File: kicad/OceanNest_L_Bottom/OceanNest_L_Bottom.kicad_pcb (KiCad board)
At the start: 2 copper layers, 103.5 x 88.7 mm, 4 parts

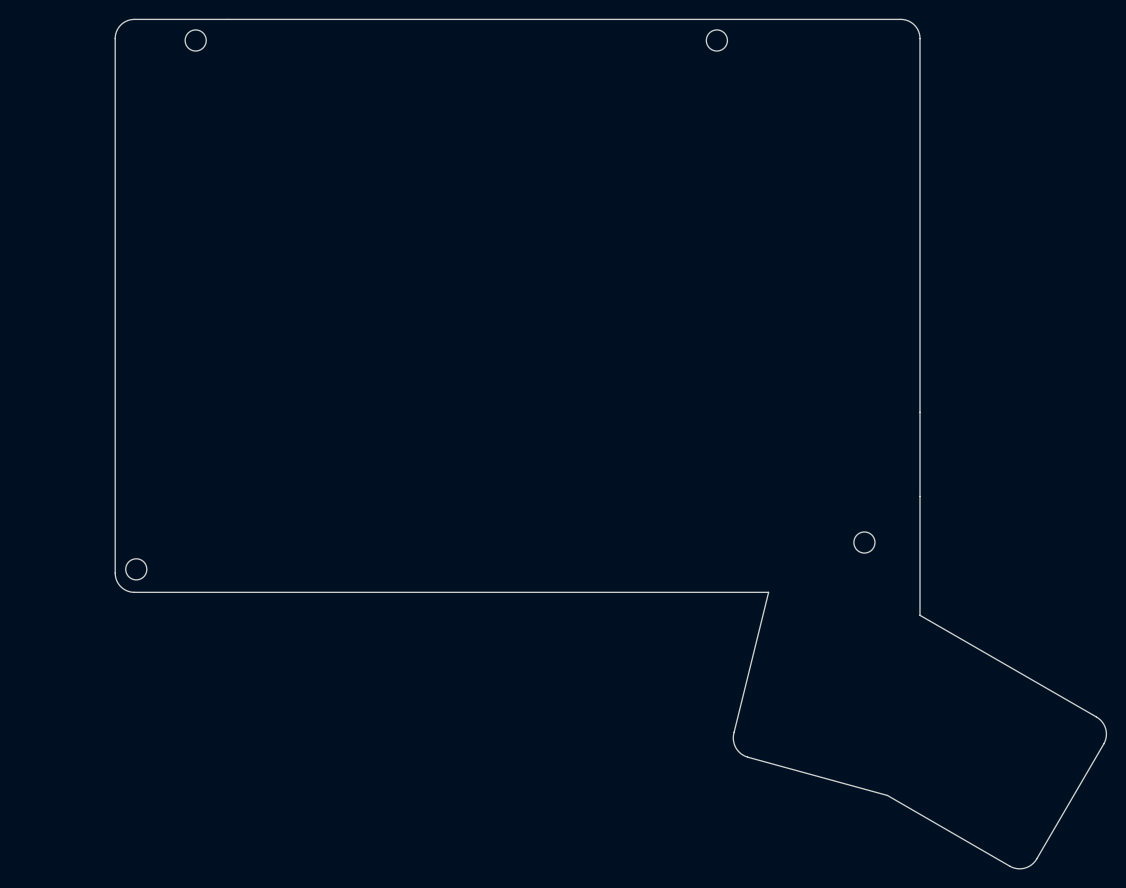
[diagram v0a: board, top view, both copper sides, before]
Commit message: feat: add new OceanNest_L and OceanNest_R PCB and project files for enhanced design capabilities
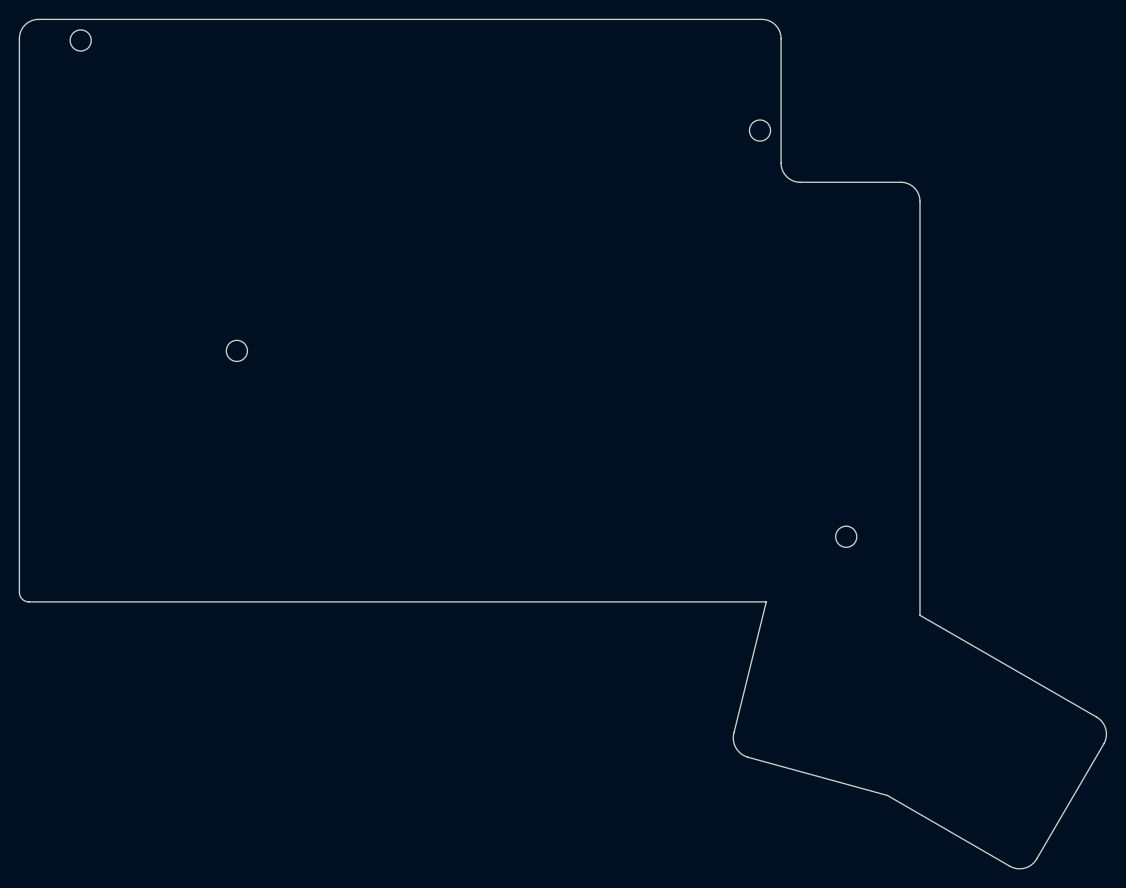
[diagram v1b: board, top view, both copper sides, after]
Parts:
- removed Ref** (x3): Val**, isw-kbd:M2_ScrewHole
- added hole2: Val**, kbd_Hole:m2_Screw_Hole, F.Cu at (72.7, 134.6)
- added hole2: Val**, kbd_Hole:m2_Screw_Hole, F.Cu at (127.3, 111.6)
- added hole2: Val**, kbd_Hole:m2_Screw_Hole, F.Cu at (56.4, 102.2)
- hole1: renamed from Ref**; footprint isw-kbd:M2_ScrewHole -> kbd_Hole:m2_Screw_Hole
- moved hole1 1.99 mm to (136.3, 154.0)
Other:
- board size 103.5 x 88.7 mm -> 113.5 x 88.7 mm
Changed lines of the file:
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@@
 	)
 	(net 0 "")
-	(footprint "isw-kbd:M2_ScrewHole"
+	(footprint "kbd_Hole:m2_Screw_Hole"
 		(layer "F.Cu")
-		(at 62.2 157.4)
+		(at 72.7 134.6)
 		(descr "Mounting Hole 2.2mm, no annular, M2")
 		(tags "mounting hole 2.2mm no annular m2")
-		(property "Reference" "Ref**"
-			(at 0 3 0)
-			(layer "F.Fab")
-			(hide yes)
+		(property "Reference" "hole2"
+			(at 0 -3.2 0)
+			(layer "F.Fab")
 			(effects
 				(font
@@
 		)
 		(property "Value" "Val**"
-			(at 0 -3 0)
-			(layer "F.Fab")
-			(hide yes)
+			(at 0 3.2 0)
+			(layer "F.Fab")
 			(effects
 				(font
@@
 		(fp_circle
 			(center 0 0)
-			(end 2 0)
+			(end 2.2 0)
 			(stroke
 				(width 0.15)
@@
 			)
 			(fill no)
-			(layer "B.Fab")
+			(layer "Cmts.User")
+		)
+		(fp_circle
+			(center 0 0)
+			(end 2.45 0)
+			(stroke
+				(width 0.05)
+				(type solid)
+			)
+			(fill no)
+			(layer "F.CrtYd")
 		)
 		(fp_text user "${REFERENCE}"
@@
 		(embedded_fonts no)
 	)
-	(footprint "isw-kbd:M2_ScrewHole"
+	(footprint "kbd_Hole:m2_Screw_Hole"
 		(layer "F.Cu")
-		(at 138.2 154.6)
+		(at 127.3 111.6)
 		(descr "Mounting Hole 2.2mm, no annular, M2")
 		(tags "mounting hole 2.2mm no annular m2")
-		(property "Reference" "Ref**"
-			(at 0 3 0)
-			(layer "F.Fab")
-			(hide yes)
+		(property "Reference" "hole2"
+			(at 0 -3.2 0)
+			(layer "F.Fab")
 			(effects
 				(font
@@
 		)
 		(property "Value" "Val**"
-			(at 0 -3 0)
-			(layer "F.Fab")
-			(hide yes)
+			(at 0 3.2 0)
+			(layer "F.Fab")
 			(effects
 				(font
@@
 		(fp_circle
 			(center 0 0)
-			(end 2 0)
+			(end 2.2 0)
 			(stroke
 				(width 0.15)
@@
 			)
 			(fill no)
-			(layer "B.Fab")
+			(layer "Cmts.User")
+		)
+		(fp_circle
+			(center 0 0)
+			(end 2.45 0)
+			(stroke
+				(width 0.05)
+				(type solid)
+			)
+			(fill no)
+			(layer "F.CrtYd")
 		)
 		(fp_text user "${REFERENCE}"
@@
 		(embedded_fonts no)
 	)
-	(footprint "isw-kbd:M2_ScrewHole"
+	(footprint "kbd_Hole:m2_Screw_Hole"
 		(layer "F.Cu")
-		(at 68.4 102.2)
+		(at 136.3 154)
 		(descr "Mounting Hole 2.2mm, no annular, M2")
 		(tags "mounting hole 2.2mm no annular m2")
-		(property "Reference" "Ref**"
-			(at 0 3 0)
-			(layer "F.Fab")
-			(hide yes)
+		(property "Reference" "hole1"
+			(at 0 -3.2 0)
+			(layer "F.Fab")
 			(effects
 				(font
@@
 		)
 		(property "Value" "Val**"
-			(at 0 -3 0)
-			(layer "F.Fab")
-			(hide yes)
+			(at 0 3.2 0)
+			(layer "F.Fab")
 			(effects
 				(font
@@
 		(fp_circle
 			(center 0 0)
-			(end 2 0)
+			(end 2.2 0)
 			(stroke
 				(width 0.15)
@@
 			)
 			(fill no)
-			(layer "B.Fab")
+			(layer "Cmts.User")
+		)
+		(fp_circle
+			(center 0 0)
+			(end 2.45 0)
+			(stroke
+				(width 0.05)
+				(type solid)
+			)
+			(fill no)
+			(layer "F.CrtYd")
 		)
 		(fp_text user "${REFERENCE}"
@@
 		(embedded_fonts no)
 	)
-	(footprint "isw-kbd:M2_ScrewHole"
+	(footprint "kbd_Hole:m2_Screw_Hole"
 		(layer "F.Cu")
-		(at 122.8 102.2)
+		(at 56.4 102.2)
 		(descr "Mounting Hole 2.2mm, no annular, M2")
 		(tags "mounting hole 2.2mm no annular m2")
-		(property "Reference" "Ref**"
-			(at 0 3 0)
-			(layer "F.Fab")
-			(hide yes)
+		(property "Reference" "hole2"
+			(at 0 -3.2 0)
+			(layer "F.Fab")
 			(effects
 				(font
@@
 		)
 		(property "Value" "Val**"
-			(at 0 -3 0)
-			(layer "F.Fab")
-			(hide yes)
+			(at 0 3.2 0)
+			(layer "F.Fab")
 			(effects
 				(font
@@
 		(fp_circle
 			(center 0 0)
-			(end 2 0)
+			(end 2.2 0)
 			(stroke
 				(width 0.15)
@@
 			)
 			(fill no)
-			(layer "B.Fab")
+			(layer "Cmts.User")
+		)
+		(fp_circle
+			(center 0 0)
+			(end 2.45 0)
+			(stroke
+				(width 0.05)
+				(type solid)
+			)
+			(fill no)
+			(layer "F.CrtYd")
 		)
 		(fp_text user "${REFERENCE}"
@@
 	)
 	(gr_arc
+		(start 127.5 100)
+		(mid 128.914214 100.585786)
+		(end 129.5 102)
+		(stroke
+			(width 0.05)
+			(type default)
+		)
+		(layer "Edge.Cuts")
+	)
+	(gr_arc
+		(start 131.5 117)
+		(mid 130.085786 116.414214)
+		(end 129.5 115)
+		(stroke
+			(width 0.05)
+			(type default)
+		)
+		(layer "Edge.Cuts")
+	)
+	(gr_arc
+		(start 142 117)
+		(mid 143.414214 117.585786)
+		(end 144 119)
+		(stroke
+			(width 0.05)
+			(type default)
+		)
+		(layer "Edge.Cuts")
+	)
+	(gr_arc
 		(start 126 177.000002)
 		(mid 124.761527 175.989951)
@@
 	)
 	(gr_line
-		(start 142 100)
-		(end 71.8 100)
-		(stroke
-			(width 0.05)
-			(type default)
-		)
-		(layer "Edge.Cuts")
-	)
-	(gr_line
-		(start 144 102)
-		(end 144 141)
+		(start 127.5 100)
+		(end 53 100)
+		(stroke
+			(width 0.05)
+			(type default)
+		)
+		(layer "Edge.Cuts")
+	)
+	(gr_line
+		(start 144 119)
+		(end 144 162.2)
 		(stroke
 			(width 0.05)
@@
 		(layer "Edge.Cuts")
 	)
-	(gr_arc
-		(start 62 159.8)
-		(mid 60.585786 159.214214)
-		(end 60 157.8)
+	(gr_line
+		(start 52 100)
+		(end 53 100)
 		(stroke
 			(width 0.05)
@@
 	)
 	(gr_line
-		(start 62 159.8)
-		(end 128.2 159.8)
+		(start 51 160.8)
+		(end 127.953425 160.799999)
 		(stroke
 			(width 0.05)
@@
 	(gr_line
 		(start 124.6 174.400002)
-		(end 128.2 159.8)
+		(end 127.953425 160.799999)
 		(stroke
 			(width 0.05)
@@
 	)
 	(gr_line
-		(start 60 157.8)
-		(end 60 102)
-		(stroke
-			(width 0.05)
-			(type default)
-		)
-		(layer "Edge.Cuts")
-	)
-	(gr_line
-		(start 144 141)
-		(end 144 149.8)
-		(stroke
-			(width 0.05)
-			(type default)
-		)
-		(layer "Edge.Cuts")
-	)
-	(gr_arc
-		(start 60 102)
-		(mid 60.585781 100.585772)
-		(end 62 100)
-		(stroke
-			(width 0.05)
-			(type default)
-		)
-		(layer "Edge.Cuts")
-	)
-	(gr_arc
-		(start 142 100)
-		(mid 143.414214 100.585786)
-		(end 144 102)
+		(start 50 159.8)
+		(end 50 102)
+		(stroke
+			(width 0.05)
+			(type default)
+		)
+		(layer "Edge.Cuts")
+	)
+	(gr_line
+		(start 142 117)
+		(end 131.5 117)
+		(stroke
+			(width 0.05)
+			(type default)
+		)
+		(layer "Edge.Cuts")
+	)
+	(gr_arc
+		(start 51 160.8)
+		(mid 50.292893 160.507107)
+		(end 50 159.8)
+		(stroke
+			(width 0.05)
+			(type default)
+		)
+		(layer "Edge.Cuts")
+	)
+	(gr_arc
+		(start 50 102)
+		(mid 50.585781 100.585772)
+		(end 52 100)
 		(stroke
 			(width 0.05)
@@
 		(layer "Edge.Cuts")
 	)
-	(gr_line
-		(start 143.999998 162.200001)
-		(end 144 149.8)
-		(stroke
-			(width 0.05)
-			(type default)
-		)
-		(layer "Edge.Cuts")
-	)
 	(gr_arc
 		(start 156.199998 187.600001)
@@
 	)
 	(gr_line
-		(start 71.8 100)
-		(end 62 100)
-		(stroke
-			(width 0.05)
+		(start 129.5 115)
+		(end 129.5 102)
+		(stroke
+			(width 0.05)
